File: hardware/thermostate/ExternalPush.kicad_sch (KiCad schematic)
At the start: 4 parts

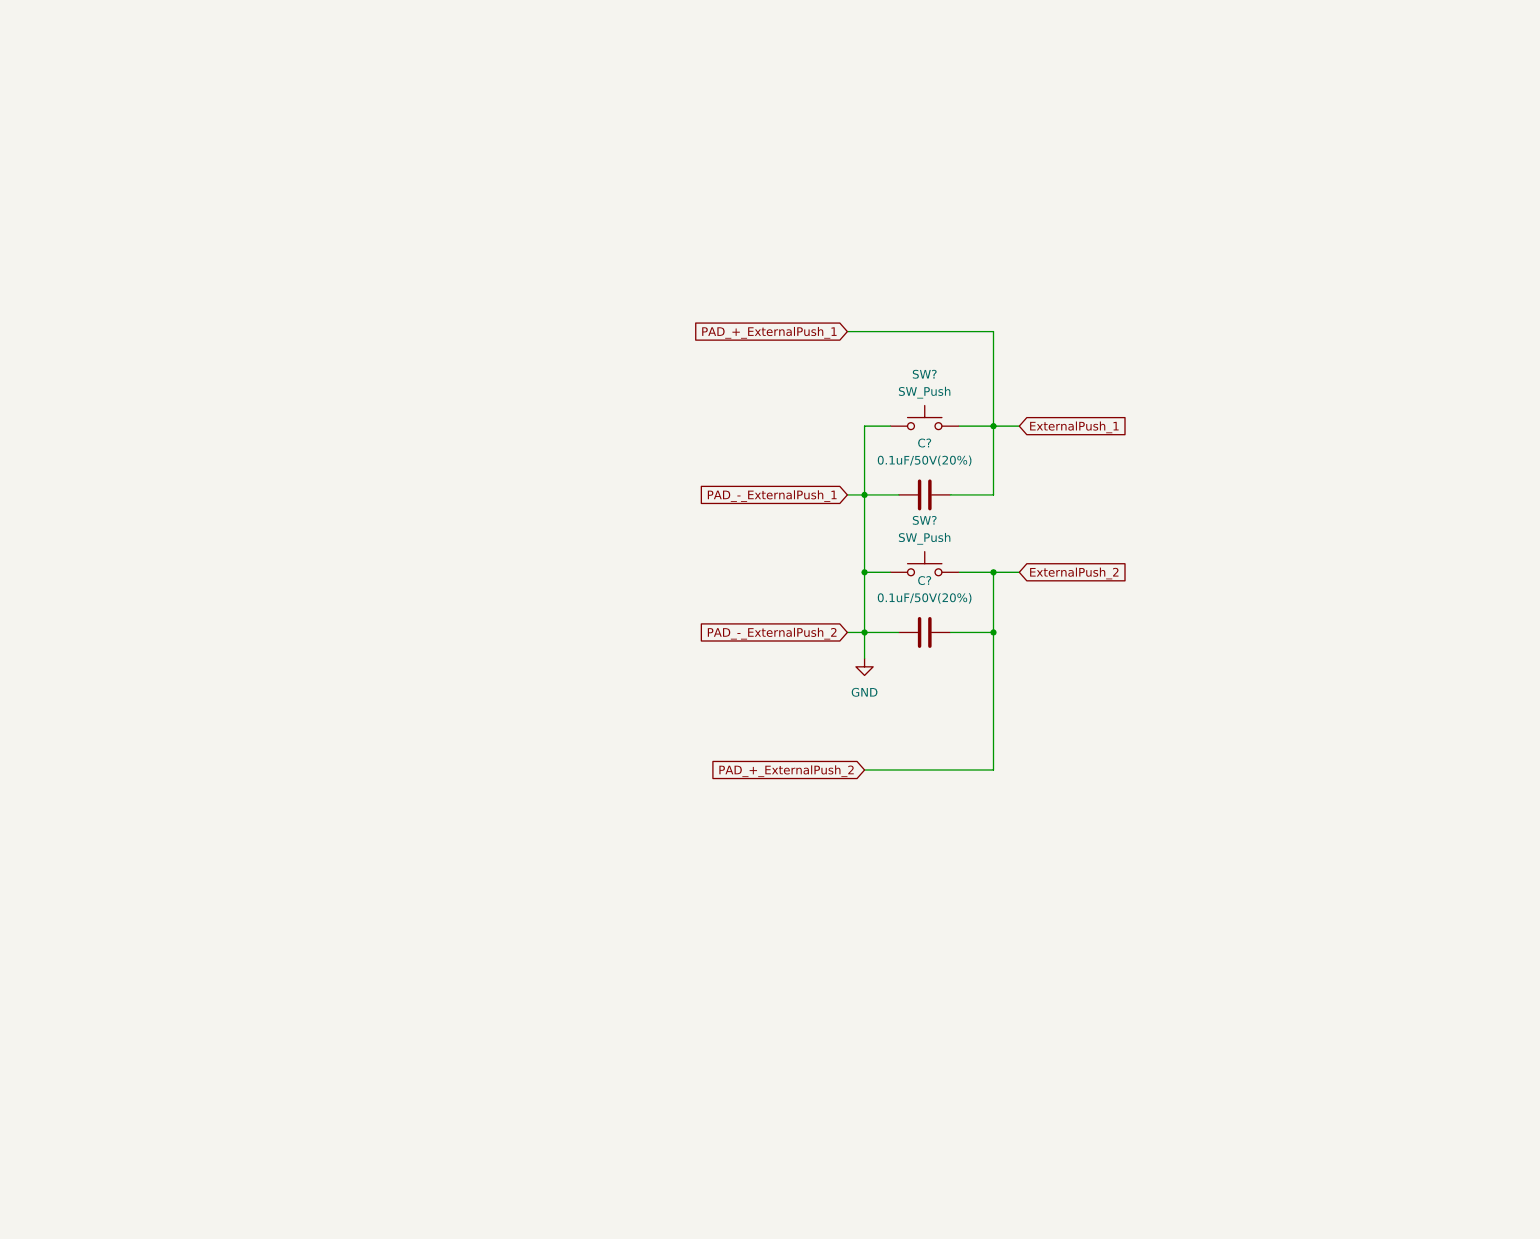
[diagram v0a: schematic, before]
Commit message: Add temperature sensor
Signed-off-by: Javier <javierfernandezvillasante@gmail.com>
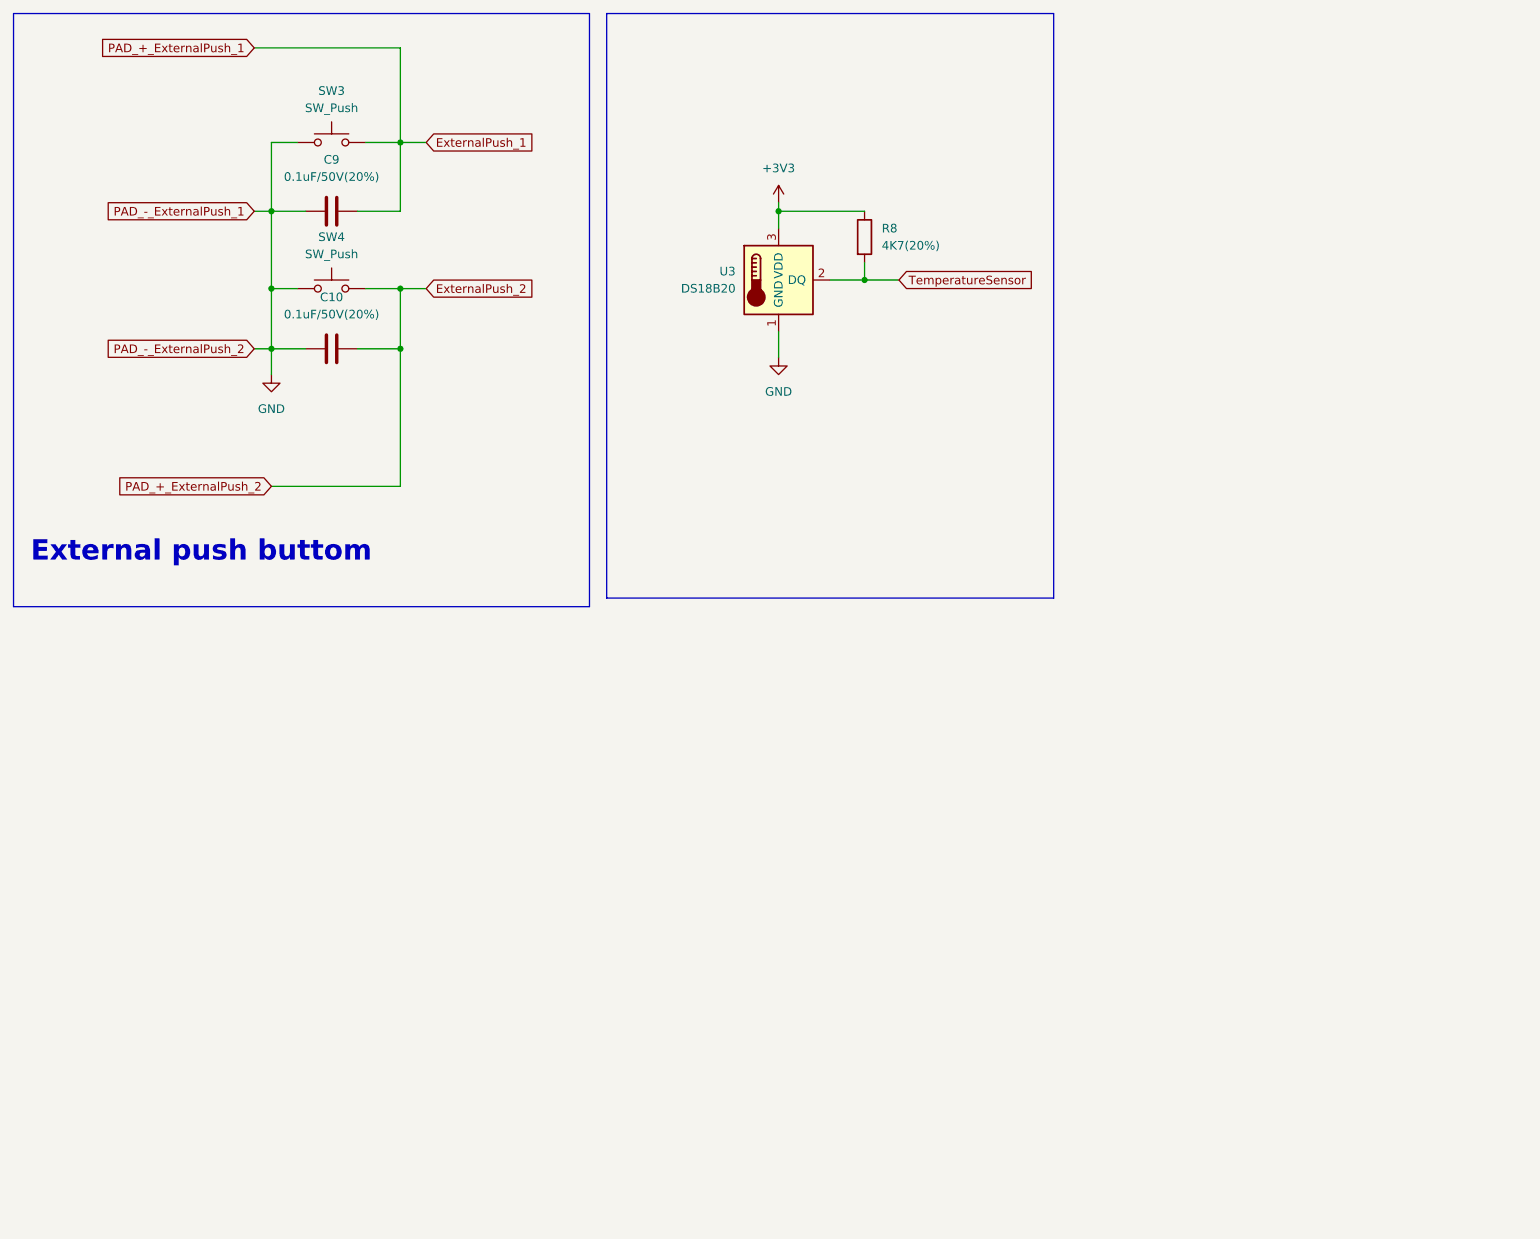
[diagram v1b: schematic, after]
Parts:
- added R8: 4K7(20%), Resistor_SMD:R_0805_2012Metric_Pad1.20x1.40mm_HandSolder, symbol Device:R
- added U3: DS18B20, Package_TO_SOT_THT:TO-92_Inline, symbol Sensor_Temperature:DS18B20
- gave numbers to parts that had none: 4
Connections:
- net GND: now also U3.1 (GND)
- new net +3V3: R8.1, U3.3 (VDD)
- new net TemperatureSensor: R8.2, U3.2 (DQ)
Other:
- note added: "External push buttom"
- moved on the sheet: C10, C9, SW3, SW4

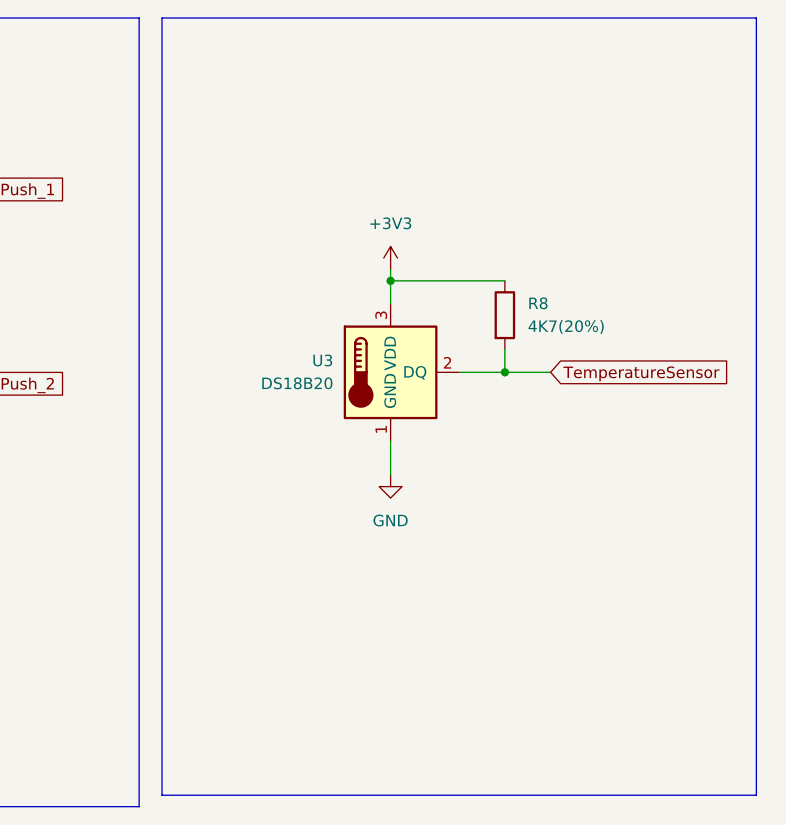
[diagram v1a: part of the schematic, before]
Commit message: Add Components PCB
Signed-off-by: Javier <javierfernandezvillasante@gmail.com>
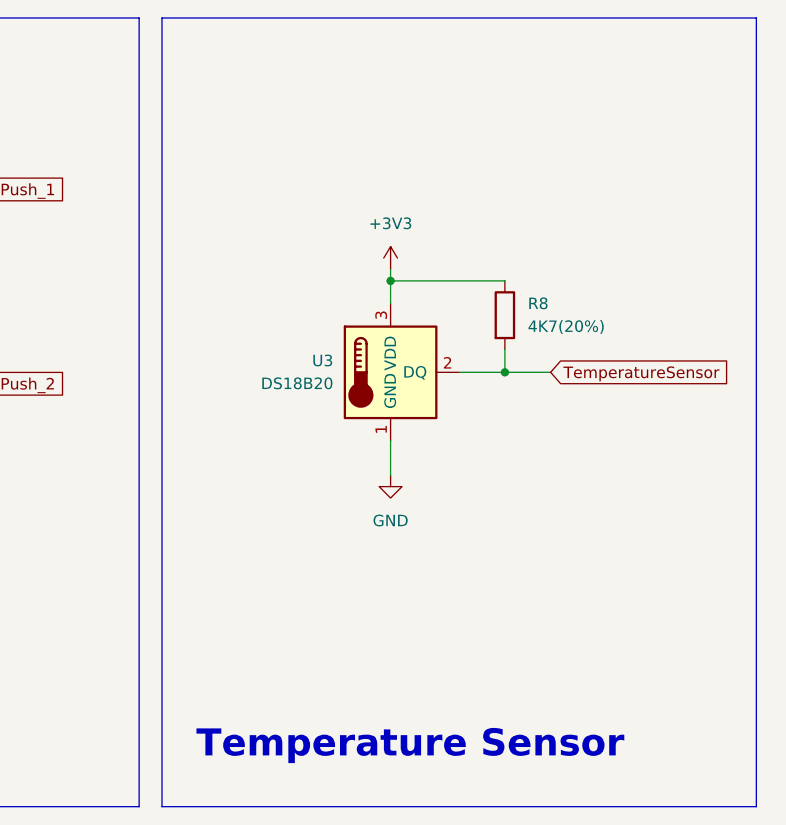
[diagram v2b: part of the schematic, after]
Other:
- note added: "Temperature Sensor"
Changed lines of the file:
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@@
     (stroke (width 0) (type default) (color 0 0 0 0))
   )
-  (polyline (pts (xy 167.64 99.06) (xy 167.64 12.7))
+  (polyline (pts (xy 167.64 100.33) (xy 167.64 12.7))
     (stroke (width 0) (type default) (color 0 0 0 0))
   )
@@
     (stroke (width 0) (type default) (color 0 0 0 0))
   )
-  (polyline (pts (xy 101.6 99.06) (xy 167.64 99.06))
+  (polyline (pts (xy 101.6 100.33) (xy 167.64 100.33))
     (stroke (width 0) (type default) (color 0 0 0 0))
   )
@@
     (stroke (width 0) (type default) (color 0 0 0 0))
   )
-  (polyline (pts (xy 101.6 12.7) (xy 101.6 99.06))
+  (polyline (pts (xy 101.6 12.7) (xy 101.6 100.33))
     (stroke (width 0) (type default) (color 0 0 0 0))
   )
+  (text "Temperature Sensor\n" (at 105.41 95.25 0)
+    (effects (font (size 3 3) (thickness 1) bold) (justify left bottom))
+  )
   (text "External push buttom" (at 16.51 93.98 0)

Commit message: Start desing PCB
Signed-off-by: Javier <javierfernandezvillasante@gmail.com>
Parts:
- added J1, J2: Conn_01x02_Male, TerminalBlock_MetzConnect:TerminalBlock_MetzConnect_360291_1x01_Horizontal_ScrewM3.0_Boxed, symbol Connector:Conn_01x02_Male
- added K1: SRD-03VDC-SL-C, SRD-03VDC-SL-C:SRD03VDCSLC, symbol SRD-03VDC-SL-C:SRD-03VDC-SL-C
- added R11: RK09K1130A5R, RK09K1130A5R:RK09K1130A5R, symbol RK09K1130A5R:RK09K1130A5R
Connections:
- net +3V3: now also R11.1
- net ExternalPush_1: now also SW3.1, J1.1 (Pin_1)
- net GND: now also J1.2 (Pin_2), J2.2 (Pin_2), R11.3, R11.4, R11.5; no longer SW3.1, SW4.1
- new net: J2.1 (Pin_1), SW4.1
- new net AC: K1.1 (COIL_1)
- new net GND1: K1.3 (COM_1)
- new net Potenciometro: R11.2
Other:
- note added: "POTENCIOMETER"

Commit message: Add SCH with low power components
Signed-off-by: Javier <javierfernandezvillasante@gmail.com>
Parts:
- added BT1: BC2AAAPC, BC2AAAPC:BAT_BC2AAAPC, symbol BC2AAAPC:BC2AAAPC
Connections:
- net GND: now also BT1.-
- new net BatterySupply: BT1.+
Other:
- note added: "Battery Supply"
- note added: "HIGH TENSION"
- moved on the sheet: K1

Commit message: New PCB desing
Signed-off-by: Javier <javierfernandezvillasante@gmail.com>
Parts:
- added D7: 1N4148W, Diode_SMD:D_SOD-123, symbol Diode:1N4148W
- added P2: 1929517, phoenix_terminalBlock:PHOENIX_1929517, symbol 1929517:1929517
- added U4: IRLML2502TRPBF, Package_TO_SOT_SMD:SOT-23, symbol IRLML2502TRPBF:IRLML2502TRPBF
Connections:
- net +3V3: now also U4.2
- net AC: now also P2.2.1 (2), P2.2.2 (2)
- net GND: now also K1.5 (COM_2), D7.2 (A)
- net GND1: now also P2.1.1 (1), P2.1.2 (1)
- net at K1.4 (COIL_2): now also D7.1 (K), U4.3
- new net RelayControlSignal: U4.1
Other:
- moved on the sheet: K1

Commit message: Stop until next winter
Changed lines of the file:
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@@
   (junction (at 139.7 52.07) (diameter 0) (color 0 0 0 0)
   )
-  (junction (at 71.12 62.23) (diameter 0) (color 0 0 0 0)
-  )
   (junction (at 127 41.91) (diameter 0) (color 0 0 0 0)
   )
@@
   (junction (at 113.03 151.13) (diameter 0) (color 0 0 0 0)
   )
-  (wire (pts (xy 52.07 82.55) (xy 71.12 82.55))
-    (stroke (width 0) (type default) (color 0 0 0 0))
-  )
   (polyline (pts (xy 99.06 100.33) (xy 13.97 100.33))
     (stroke (width 0) (type default) (color 0 0 0 0))
@@
   )
   (polyline (pts (xy 99.06 12.7) (xy 99.06 100.33))
-    (stroke (width 0) (type default) (color 0 0 0 0))
-  )
-  (wire (pts (xy 71.12 82.55) (xy 71.12 62.23))
     (stroke (width 0) (type default) (color 0 0 0 0))
   )
@@
     )
   )
-  (global_label "PAD_+_ExternalPush_2" (shape input) (at 52.07 82.55 180) (fields_autoplaced)
-    (effects (font (size 1.27 1.27)) (justify right))
-    (property "Intersheet References" "${INTERSHEET_REFS}" (id 0) (at 28.0064 82.4706 0)
-      (effects (font (size 1.27 1.27)) (justify right) hide)
-    )
-  )
